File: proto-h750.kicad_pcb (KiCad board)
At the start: 2 copper layers, 63.5 x 73.7 mm, 64 parts, among them J1 Micro_SD_Card, J2 USB_B_Micro, J3 USB_B_Micro, J4 Conn_02x14_Odd_Even, J5 Conn_02x14_Odd_Even, J6 Conn_02x08_Odd_Even, J7 Conn_02x02_Odd_Even, J8 USB_B_Micro, J9 Conn_02x04_Odd_Even, SW1 SW_Push, SW2 SW_Push, SW3 SW_DIP_x01, U1 S25FL132K0XMFI010, U2 STM32H750VBT6, U3 AP1117-33, U4 KSZ8081RNA, Y1 16MHz, Y2 32.768KHz

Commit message: More TX
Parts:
- added REF** (x4): SOP65P1420X343-36N, SOP65P1420X343-36N, F.Cu at (0.00, 0.00)

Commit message: Before deleting Flash
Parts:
- removed REF** (x4): SOP65P1420X343-36N, SOP65P1420X343-36N
- added C25: 10n, Capacitor_SMD:C_0805_2012Metric_Pad1.15x1.40mm_HandSolder, F.Cu at (202.1, 56.4)
- added C26: 100n, Capacitor_SMD:C_0805_2012Metric_Pad1.15x1.40mm_HandSolder, F.Cu at (170.2, 150.4)
- added C27: 220n, Capacitor_SMD:C_0805_2012Metric_Pad1.15x1.40mm_HandSolder, F.Cu at (170.2, 153.4)
- added C28: 100n, Capacitor_SMD:C_0805_2012Metric_Pad1.15x1.40mm_HandSolder, F.Cu at (168.9, 158.1)
- added C29: 100n, Capacitor_SMD:C_0805_2012Metric_Pad1.15x1.40mm_HandSolder, F.Cu at (174.9, 150.4)
- added C30: 1u, Capacitor_SMD:C_0805_2012Metric_Pad1.15x1.40mm_HandSolder, F.Cu at (174.9, 153.4)
- added C31: 100n, Capacitor_SMD:C_0805_2012Metric_Pad1.15x1.40mm_HandSolder, F.Cu at (168.9, 161.0)
- added C32: 100n, Capacitor_SMD:C_0805_2012Metric_Pad1.15x1.40mm_HandSolder, F.Cu at (173.6, 156.3)
- added C33: 220n, Capacitor_SMD:C_0805_2012Metric_Pad1.15x1.40mm_HandSolder, F.Cu at (173.6, 159.3)
- added C34: 1u, Capacitor_SMD:C_0805_2012Metric_Pad1.15x1.40mm_HandSolder, F.Cu at (168.9, 164.0)
- added C35: 330p, Capacitor_SMD:C_0805_2012Metric_Pad1.15x1.40mm_HandSolder, F.Cu at (178.4, 156.3)
- added C36: 220u, Capacitor_SMD:CP_Elec_8x10, F.Cu at (160.7, 161.5)
- added C37: 100n, Capacitor_SMD:C_0805_2012Metric_Pad1.15x1.40mm_HandSolder, F.Cu at (176.1, 146.2)
- added C38: 100n, Capacitor_SMD:C_0805_2012Metric_Pad1.15x1.40mm_HandSolder, F.Cu at (173.6, 162.2)
- added C39: 220n polyester, Capacitor_SMD:C_1812_4532Metric_Pad1.30x3.40mm_HandSolder, F.Cu at (143.9, 160.8)
- added C40: 10n, Capacitor_SMD:C_0805_2012Metric_Pad1.15x1.40mm_HandSolder, F.Cu at (131.0, 155.1)
- added C41: C, Capacitor_SMD:C_0805_2012Metric_Pad1.15x1.40mm_HandSolder, F.Cu at (122.8, 161.5)
- added C42: 10n, Capacitor_SMD:C_0805_2012Metric_Pad1.15x1.40mm_HandSolder, F.Cu at (126.2, 158.0)
- added C43: 10p, Capacitor_SMD:C_0805_2012Metric_Pad1.15x1.40mm_HandSolder, F.Cu at (132.2, 152.1)
- added C44: 100n, Capacitor_SMD:C_0805_2012Metric_Pad1.15x1.40mm_HandSolder, F.Cu at (118.0, 164.5)
- added C45: 100n, Capacitor_SMD:C_0805_2012Metric_Pad1.15x1.40mm_HandSolder, F.Cu at (131.2, 146.2)
- added C46: 100n, Capacitor_SMD:C_0805_2012Metric_Pad1.15x1.40mm_HandSolder, F.Cu at (113.3, 163.2)
- added C47: 100n, Capacitor_SMD:C_0805_2012Metric_Pad1.15x1.40mm_HandSolder, F.Cu at (121.5, 155.6)
- added C48: 10n, Capacitor_SMD:C_0805_2012Metric_Pad1.15x1.40mm_HandSolder, F.Cu at (127.5, 152.1)
- added C49: 0, Capacitor_SMD:C_0805_2012Metric_Pad1.15x1.40mm_HandSolder, F.Cu at (113.3, 166.2)
- added C50: 100n, Capacitor_SMD:C_0805_2012Metric_Pad1.15x1.40mm_HandSolder, F.Cu at (121.5, 158.6)
- added C51: 10n, Capacitor_SMD:C_0805_2012Metric_Pad1.15x1.40mm_HandSolder, F.Cu at (131.2, 149.2)
- added C52: 0, Capacitor_SMD:C_0805_2012Metric_Pad1.15x1.40mm_HandSolder, F.Cu at (118.0, 161.5)
- added C53: 10n, Capacitor_SMD:C_0805_2012Metric_Pad1.15x1.40mm_HandSolder, F.Cu at (94.3, 164.0)
- added C54: 100n, Capacitor_SMD:C_0805_2012Metric_Pad1.15x1.40mm_HandSolder, F.Cu at (94.3, 166.9)
- added C55: 10n, Capacitor_SMD:C_0805_2012Metric_Pad1.15x1.40mm_HandSolder, F.Cu at (99.0, 164.0)
- added C56: 100n, Capacitor_SMD:C_0805_2012Metric_Pad1.15x1.40mm_HandSolder, F.Cu at (107.2, 157.3)
- added C57: 10u, Capacitor_SMD:C_Elec_4x5.4, F.Cu at (101.5, 90.8)
- added C58: 1n, Capacitor_SMD:C_0805_2012Metric_Pad1.15x1.40mm_HandSolder, F.Cu at (171.5, 62.6)
- added C59: C, Capacitor_SMD:C_0805_2012Metric_Pad1.15x1.40mm_HandSolder, F.Cu at (98.1, 33.6)
- added D3: D, Diode_SMD:D_SOD-123, F.Cu at (185.6, 62.3)
- added D4: MMBD914LT3G, Diode_SMD:D_SOD-123, F.Cu at (192.1, 56.5)
- added L1: NRH3012T100MN, Inductor_SMD:L_Taiyo-Yuden_NR-30xx_HandSoldering, F.Cu at (100.8, 68.1)
- added L2: 47u SRR1210-470M, Inductor_SMD:L_Bourns_SRR1210A, F.Cu at (147.5, 151.5)
- added L3: 10u, Inductor_SMD:L_0805_2012Metric_Pad1.15x1.40mm_HandSolder, F.Cu at (126.2, 155.1)
- added L4: 10u, Inductor_SMD:L_0805_2012Metric_Pad1.15x1.40mm_HandSolder, F.Cu at (118.0, 152.7)
- added Q1: BS170, Package_TO_SOT_THT:TO-92_Inline, F.Cu at (184.7, 58.1)
- added Q2: BS170, Package_TO_SOT_THT:TO-92_Inline, F.Cu at (191.2, 52.3)
- added Q3: BS170, Package_TO_SOT_THT:TO-92_Inline, F.Cu at (184.7, 52.3)
- added Q4: IRF540N, Package_TO_SOT_THT:TO-220-3_Vertical, F.Cu at (185.9, 47.0)
- added Q5: BSS138, Package_TO_SOT_SMD:SOT-23, F.Cu at (200.2, 60.2)
- added Q6: MMBT2222, Package_TO_SOT_SMD:SOT-23, F.Cu at (130.8, 158.8)
- added R17: 0, Resistor_SMD:R_0805_2012Metric_Pad1.15x1.40mm_HandSolder, F.Cu at (113.2, 152.7)
- added R18: 10k, Resistor_SMD:R_0805_2012Metric_Pad1.15x1.40mm_HandSolder, F.Cu at (121.7, 146.2)
- added R19: 3k3, Resistor_SMD:R_0805_2012Metric_Pad1.15x1.40mm_HandSolder, F.Cu at (99.0, 166.9)
- added R20: 100, Resistor_SMD:R_0805_2012Metric_Pad1.15x1.40mm_HandSolder, F.Cu at (103.8, 164.0)
- added R21: 10k, Resistor_SMD:R_0805_2012Metric_Pad1.15x1.40mm_HandSolder, F.Cu at (107.2, 160.3)
- added R22: 10k, Resistor_SMD:R_0805_2012Metric_Pad1.15x1.40mm_HandSolder, F.Cu at (112.0, 157.3)
- added R23: 100, Resistor_SMD:R_0805_2012Metric_Pad1.15x1.40mm_HandSolder, F.Cu at (122.8, 164.5)
- added R24: 100k, Resistor_SMD:R_0805_2012Metric_Pad1.15x1.40mm_HandSolder, F.Cu at (121.7, 149.2)
- added R25: 0, Resistor_SMD:R_0805_2012Metric_Pad1.15x1.40mm_HandSolder, F.Cu at (103.8, 166.9)
- added R26: 100, Resistor_SMD:R_0805_2012Metric_Pad1.15x1.40mm_HandSolder, F.Cu at (126.4, 146.2)
- added R27: 100k, Resistor_SMD:R_0805_2012Metric_Pad1.15x1.40mm_HandSolder, F.Cu at (112.0, 160.3)
- added R28: 100, Resistor_SMD:R_0805_2012Metric_Pad1.15x1.40mm_HandSolder, F.Cu at (108.5, 163.2)
- added R29: 62k, Resistor_SMD:R_0805_2012Metric_Pad1.15x1.40mm_HandSolder, F.Cu at (118.0, 167.4)
- added R30: 150k, Resistor_SMD:R_0805_2012Metric_Pad1.15x1.40mm_HandSolder, F.Cu at (116.7, 155.6)
- added R31: 100, Resistor_SMD:R_0805_2012Metric_Pad1.15x1.40mm_HandSolder, F.Cu at (122.7, 152.1)
- added R32: 2k2, Resistor_SMD:R_0805_2012Metric_Pad1.15x1.40mm_HandSolder, F.Cu at (116.7, 158.6)
- added R33: 0, Resistor_SMD:R_0805_2012Metric_Pad1.15x1.40mm_HandSolder, F.Cu at (108.5, 166.2)
- added R34: 0, Resistor_SMD:R_0805_2012Metric_Pad1.15x1.40mm_HandSolder, F.Cu at (126.4, 149.2)
- added R35: 0, Resistor_SMD:R_1210_3225Metric_Pad1.42x2.65mm_HandSolder, F.Cu at (143.2, 165.4)
- added R36: 0, Resistor_SMD:R_1210_3225Metric_Pad1.42x2.65mm_HandSolder, F.Cu at (150.5, 160.4)
- added R37: 10k, Resistor_SMD:R_1210_3225Metric_Pad1.42x2.65mm_HandSolder, F.Cu at (126.4, 91.2)
- added R38: 10k, Resistor_SMD:R_1210_3225Metric_Pad1.42x2.65mm_HandSolder, F.Cu at (106.7, 88.9)
- added R39: 10k, Resistor_SMD:R_1210_3225Metric_Pad1.42x2.65mm_HandSolder, F.Cu at (92.8, 34.2)
- added T1: Transformer_1P_1S, Transformer_THT:Transformer_Toroid_Horizontal_D10.5mm_Amidon-T37, F.Cu at (70.5, 150.5)
- added TP2: TestPoint, TestPoint:TestPoint_Pad_2.0x2.0mm, F.Cu at (195.2, 63.2)
- added TP3: TestPoint, TestPoint:TestPoint_Pad_2.0x2.0mm, F.Cu at (135.1, 158.6)
- added TP4: TestPoint, TestPoint:TestPoint_Pad_2.0x2.0mm, F.Cu at (127.2, 167.0)
- added U10: BGA2869, Package_TO_SOT_SMD:SOT-363_SC-70-6, F.Cu at (122.5, 167.9)
- added U11: BGA2869, Package_TO_SOT_SMD:SOT-363_SC-70-6, F.Cu at (127.3, 163.0)
- added U5: LM7812_TO220, Package_TO_SOT_THT:TO-220-3_Vertical, F.Cu at (197.5, 47.0)
- added U6: LM5134AMF_NOPB, Package_TO_SOT_SMD:SOT-23-6_Handsoldering, F.Cu at (208.7, 45.4)
- added U8: STA510, Package_SO:ST_PowerSSO-36_SlugDown, F.Cu at (161.2, 150.7)
- added U9: SA612, Package_SO:SOIC-8_3.9x4.9mm_P1.27mm, F.Cu at (115.1, 148.0)
- added X1: ASV-xxxMHz, Oscillator:Oscillator_SMD_Abracon_ASV-4Pin_7.0x5.1mm, F.Cu at (98.3, 84.3)
- C1, C10, C12, C13, C14, C15, C16, C17, C18, C2, C23, C3, C4, C5, C6, C7, C8: footprint Capacitor_SMD:C_0805_2012Metric -> Capacitor_SMD:C_0805_2012Metric_Pad1.15x1.40mm_HandSolder
- C11: value 18p -> 1u; footprint Capacitor_SMD:C_0805_2012Metric -> Capacitor_SMD:C_0805_2012Metric_Pad1.15x1.40mm_HandSolder
- C19: value 100n -> 10u; footprint Capacitor_SMD:C_0805_2012Metric -> Capacitor_SMD:C_0805_2012Metric_Pad1.15x1.40mm_HandSolder
- C20: value 2.2u -> 10u; footprint Capacitor_SMD:C_0805_2012Metric -> Capacitor_SMD:C_0805_2012Metric_Pad1.15x1.40mm_HandSolder
- C21: value 4.7u -> 10u; footprint Capacitor_SMD:C_0805_2012Metric -> Capacitor_SMD:C_0805_2012Metric_Pad1.15x1.40mm_HandSolder
- C22: value 100n -> 1u; footprint Capacitor_SMD:C_0805_2012Metric -> Capacitor_SMD:C_0805_2012Metric_Pad1.15x1.40mm_HandSolder
- C24: value 4.7u -> 100n; footprint Capacitor_SMD:C_0805_2012Metric -> Capacitor_SMD:C_0805_2012Metric_Pad1.15x1.40mm_HandSolder
- C9: value 18p -> 10u; footprint Capacitor_SMD:C_0805_2012Metric -> Capacitor_SMD:C_Elec_4x5.4
- J1: value Micro_SD_Card -> Conn_02x14_Odd_Even; footprint Connector_Card:microSD_HC_Hirose_DM3AT-SF-PEJM5 -> Connector_PinHeader_2.54mm:PinHeader_2x14_P2.54mm_Vertical
- J5: value Conn_02x14_Odd_Even -> Conn_02x08_Odd_Even; footprint Connector_PinHeader_2.54mm:PinHeader_2x14_P2.54mm_Vertical -> Connector_PinHeader_2.54mm:PinHeader_2x08_P2.54mm_Vertical
- J6: value Conn_02x08_Odd_Even -> AudioJack3; footprint Connector_PinHeader_2.54mm:PinHeader_2x08_P2.54mm_Vertical -> Connector_Audio:Jack_3.5mm_CUI_SJ1-3535NG_Horizontal
- J8: value USB_B_Micro -> Conn_02x08_Odd_Even; footprint Connector_USB:USB_Micro-B_Molex-105017-0001 -> Connector_PinHeader_2.54mm:PinHeader_2x08_P2.54mm_Vertical
- J9: value Conn_02x04_Odd_Even -> AudioJack3; footprint Connector_PinHeader_2.54mm:PinHeader_2x04_P2.54mm_Vertical -> Connector_Audio:Jack_3.5mm_CUI_SJ1-3535NG_Horizontal
- R1, R16, R2, R3: footprint Resistor_SMD:R_0805_2012Metric -> Resistor_SMD:R_0805_2012Metric_Pad1.15x1.40mm_HandSolder
- R10, R12: value 0R -> 10k; footprint Resistor_SMD:R_2010_5025Metric -> Resistor_SMD:R_0805_2012Metric_Pad1.15x1.40mm_HandSolder
- R11: value 0R -> 330; footprint Resistor_SMD:R_2010_5025Metric -> Resistor_SMD:R_0805_2012Metric_Pad1.15x1.40mm_HandSolder
- R13: value 0R -> 10K; footprint Resistor_SMD:R_2010_5025Metric -> Resistor_SMD:R_0805_2012Metric_Pad1.15x1.40mm_HandSolder
- R14: value 0R -> 20 0.25W; footprint Resistor_SMD:R_2010_5025Metric -> Resistor_SMD:R_1210_3225Metric_Pad1.42x2.65mm_HandSolder
- R15: value 0R -> 6.2 0.25 W; footprint Resistor_SMD:R_2010_5025Metric -> Resistor_SMD:R_1210_3225Metric_Pad1.42x2.65mm_HandSolder
- R4, R5: value 10K -> 0; footprint Resistor_SMD:R_0805_2012Metric -> Resistor_SMD:R_0805_2012Metric_Pad1.15x1.40mm_HandSolder
- R6: value 10K -> 10k; footprint Resistor_SMD:R_0805_2012Metric -> Resistor_SMD:R_0805_2012Metric_Pad1.15x1.40mm_HandSolder
- R7: value 6.49K 1% -> 10k; footprint Resistor_SMD:R_0805_2012Metric -> Resistor_SMD:R_0805_2012Metric_Pad1.15x1.40mm_HandSolder
- R8: value 0R -> 2.2; footprint Resistor_SMD:R_2010_5025Metric -> Resistor_SMD:R_0805_2012Metric_Pad1.15x1.40mm_HandSolder
- R9: value 0R -> 1K; footprint Resistor_SMD:R_2010_5025Metric -> Resistor_SMD:R_0805_2012Metric_Pad1.15x1.40mm_HandSolder
- U4: value KSZ8081RNA -> LM7805_TO220; footprint Package_DFN_QFN:QFN-24-1EP_4x4mm_P0.5mm_EP2.6x2.6mm -> Package_TO_SOT_THT:TO-220-3_Vertical
- Y2: value 32.768KHz -> ECS-10.7-7.5B; footprint Crystal:Crystal_SMD_MicroCrystal_CC8V-T1A-2Pin_2.0x1.2mm_HandSoldering -> Crystal:Crystal_HC49-U-3Pin_Vertical
- moved H1 144.6 mm to (58.4, 149.9)
- moved R13 109.7 mm to (214.0, 44.6), turned to 0 degrees
- moved Y2 95.3 mm to (95.9, 159.2), turned to 0 degrees
- moved H3 95.1 mm to (193.9, 84.2)
- moved R8 90.8 mm to (208.2, 49.2), turned to 0 degrees
- moved R9 88.4 mm to (202.8, 50.5), turned to 0 degrees
- moved R10 85.4 mm to (198.1, 53.5), turned to 0 degrees
- moved C24 84.0 mm to (207.6, 52.2)
- moved J8 79.2 mm to (180.3, 72.4), turned to 0 degrees
- moved C22 78.1 mm to (202.8, 53.5)
- moved R11 77.8 mm to (190.8, 62.1), turned to 0 degrees
- moved R12 77.0 mm to (185.1, 65.5), turned to 0 degrees
- moved R6 76.6 mm to (198.1, 50.5), turned to 0 degrees
- moved R14 74.0 mm to (149.2, 165.4), turned to 0 degrees
- moved J6 72.3 mm to (87.6, 110.5), turned to 90 degrees
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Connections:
- C1 pad 1: VCC -> /VCC_CPU
- C10 pad 1: VCC -> /VCC_CPU
- C11 pad 1: GND -> Net-(C11-Pad1)
- C11 pad 2: Net-(C11-Pad2) -> GND
- C12 pad 1: VCC -> /VCC_CPU
- C13 pad 1: VCC -> /VCC_CPU
- C14 pad 1: GND -> Net-(C11-Pad1)
- C14 pad 2: VCC -> GND
- C15 pad 1: VCC -> /VCC_CPU
- C19 pad 1: GND -> +24V
- C19 pad 2: Net-(C19-Pad2) -> GND
- C20 pad 1: GND -> Net-(C20-Pad1)
- C20 pad 2: Net-(C20-Pad2) -> GND
- C21 pad 1: GND -> +24V
- C21 pad 2: Net-(C20-Pad2) -> GND
- C22 pad 1: GND -> /TX/+12V
- C22 pad 2: VCC -> GND
- C23 pad 1: GND -> /TX/+12V
- C23 pad 2: VCC -> GND
- C24 pad 1: GND -> /TX/+12V
- C24 pad 2: VCC -> GND
- C4 pad 1: VCC -> /VCC_CPU
- C7 pad 1: VCC -> /VCC_CPU
- C8 pad 1: VCC -> /VCC_CPU
- C9 pad 1: GND -> /AudioOut
- J1 pad 1: Net-(J1-Pad1) -> /PC0
- J1 pad 10: (no net) -> /PA5
- J1 pad 11: (no net) -> /PA6
- J1 pad 2: Net-(J1-Pad2) -> /PC1
- J1 pad 3: /SD_CMD -> /PC2
- J1 pad 4: VCC -> TXV
- J1 pad 5: /SD_CK -> /PA0
- J1 pad 6: GND -> /PA1
- J1 pad 7: /SD_D0 -> /PA2
- J1 pad 8: Net-(J1-Pad8) -> /PA3
- J1 pad 9: GND -> /AudioOut
- J2 pad 1: +5V -> Net-(J2-Pad1)
- J2 pad 4: Net-(J2-Pad4) -> (no net)
- J3 pad 1: +5V -> Net-(J2-Pad1)
- J3 pad 4: Net-(J3-Pad4) -> (no net)
- J4 pad 1: /PC0 -> GND
- J4 pad 10: /PA5 -> TX_ENA
- J4 pad 11: /PA6 -> /PE1
- J4 pad 12: /PA7 -> RXTX
- J4 pad 13: /PC4 -> /PB9
- J4 pad 14: /PC5 -> /PB8
- J4 pad 15: /PB0 -> /PB7
- J4 pad 16: /PB1 -> /PB6
- J4 pad 17: /PE11 -> /PB5
- J4 pad 18: /PE12 -> /PB4
- J4 pad 19: /PE13 -> /PB3
- J4 pad 2: /ENET_MDC -> +5V
- J4 pad 20: /PE14 -> /PD7
- J4 pad 21: /PE15 -> /PD6
- J4 pad 22: /PB10 -> /PD5
- J4 pad 23: /PB11 -> /PD4
- J4 pad 24: /PB12 -> /PD3
- J4 pad 25: /PB13 -> /PD1
- J4 pad 26: GND -> /PD0
- J4 pad 27: GND -> /PC10
- J4 pad 28: GND -> /PA15
- J4 pad 3: /PC2 -> VCC
- J4 pad 4: /PC3 -> /nRESET
- J4 pad 5: /PA0 -> VCC
- J4 pad 6: /PA1 -> /PE6
- J4 pad 7: /ENET_MDIO -> /PE5
- J4 pad 8: /PA3 -> /PE4
- J4 pad 9: /PA4 -> /PE3
- J5 pad 1: GND -> /PA9
- J5 pad 10: /PE2 -> /PD13
- J5 pad 11: /PE1 -> /PD10
- J5 pad 12: /PE0 -> /PD11
- J5 pad 13: /PB9 -> /PD8
- J5 pad 14: /PB8 -> /PD9
- J5 pad 15: /PB7 -> GND
- J5 pad 16: /PB6 -> GND
- J5 pad 2: +5V -> /PA10
- J5 pad 3: VCC -> MCO
- J5 pad 4: /nRESET -> /PA8
- J5 pad 5: VCC -> A_PWM
- J5 pad 6: /PE6 -> /PC7
- J5 pad 7: /PE5 -> /PD14
- J5 pad 8: /PE4 -> /PD15
- J5 pad 9: /PE3 -> /PD12
- J8 pad 1: +5V -> +24V
- J8 pad 2: Net-(J8-Pad2) -> (no net)
- J8 pad 3: Net-(J8-Pad3) -> +24V
- J8 pad 4: Net-(J8-Pad4) -> (no net)
- J8 pad 5: GND -> MODUL_OUT
- J8 pad 6: GND -> (no net)
- R10 pad 1: /ENET_TXD1 -> Net-(J8-Pad11)
- R10 pad 2: /PB13 -> Net-(D3-Pad2)
- R11 pad 1: /ENET_RXD0 -> Net-(D3-Pad2)
- R11 pad 2: /PC4 -> GND
- R12 pad 1: /ENET_RXD1 -> TXV
- R12 pad 2: /PA5 -> GND
- R13 pad 1: Net-(R13-Pad1) -> RXTX
- R13 pad 2: /PA7 -> GND
- R14 pad 1: /ENET_CLK -> Net-(L2-Pad1)
- R14 pad 2: /PA1 -> Net-(C35-Pad1)
- R15 pad 1: Net-(R13-Pad1) -> MODUL_OUT
- R15 pad 2: /ENET_CRSDV -> Net-(C37-Pad1)
- R4 pad 1: VCC -> Net-(J2-Pad1)
- R4 pad 2: /ENET_MDIO -> +5V
- R5 pad 1: VCC -> +5V
- R5 pad 2: /ENET_MDC -> Net-(C20-Pad1)
- R6 pad 2: Net-(C19-Pad2) -> TX_ENA
- R7 pad 1: GND -> MCO
- R7 pad 2: Net-(R7-Pad2) -> GND
- R8 pad 1: /ENET_TXEN -> Net-(C59-Pad2)
- R8 pad 2: /PB11 -> Net-(R8-Pad2)
- R9 pad 1: /ENET_TXD0 -> Net-(C59-Pad1)
- R9 pad 2: /PB12 -> GND
- U1 pad 8: VCC -> /VCC_CPU
- U2 pad 1: /PE2 -> TX_ENA
- U2 pad 100: VCC -> /VCC_CPU
- U2 pad 11: VCC -> /VCC_CPU
- U2 pad 16: /ENET_MDC -> /PC1
- U2 pad 18: /PC3 -> TXV
- U2 pad 20: VCC -> Net-(C11-Pad1)
- U2 pad 21: VCC -> /VCC_CPU
- U2 pad 24: /ENET_MDIO -> /PA2
- U2 pad 27: VCC -> /VCC_CPU
- U2 pad 28: /PA4 -> /AudioOut
- U2 pad 31: /PA7 -> /Microphone
- U2 pad 35: /PB1 -> RF_ADC_IN
- U2 pad 41: /PE11 -> A_PWM
- U2 pad 42: /PE12 -> A_PWRDN
- U2 pad 43: /PE13 -> A_FAULT
- U2 pad 50: VCC -> /VCC_CPU
- U2 pad 6: VCC -> /VCC_CPU
- U2 pad 63: /PC6 -> A_PWM
- U2 pad 65: /SD_D0 -> (no net)
- U2 pad 66: /PC9 -> MCO
- U2 pad 75: VCC -> /VCC_CPU
- U2 pad 8: Net-(C11-Pad2) -> (no net)
- U2 pad 80: /SD_CK -> (no net)
- U2 pad 83: /SD_CMD -> (no net)
- U2 pad 9: Net-(C9-Pad2) -> (no net)
- U2 pad 97: /PE0 -> RXTX
- U4 pad 1: Net-(C20-Pad2) -> +24V
- U4 pad 2: VCC -> GND
- U4 pad 3: /ETH_RX- -> Net-(C20-Pad1)
- Y1 pad 2: Net-(Y1-Pad2) -> (no net)
- Y1 pad 4: Net-(Y1-Pad4) -> (no net)
- Y2 pad 1: Net-(C11-Pad2) -> Net-(C48-Pad1)
- Y2 pad 2: Net-(C9-Pad2) -> GND
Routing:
- net VCC: track 221.0 -> 27.9 mm, vias 7 -> 0
- net +5V: track 127.9 -> 27.2 mm, vias 6 -> 0
- net /ENET_MDC: track 80.3 -> 0.00 mm
- net /ENET_MDIO: track 70.6 -> 0.00 mm
- net GND: track 127.8 -> 183.8 mm, vias 44 -> 19
- net /BOOT: track 46.8 -> 0.00 mm, vias 2 -> 0
- net /ENET_CLK: track 46.1 -> 0.00 mm
- net /VCC_CPU: track 0.00 -> 44.9 mm
- net /PB13: track 40.0 -> 0.00 mm
- net /PB12: track 35.0 -> 0.00 mm
- net /PC0: track 34.9 -> 0.00 mm
- net /USB0_D+: track 34.8 -> 0.00 mm
- net /USB0_D-: track 34.7 -> 0.00 mm
- net /PA1: track 32.5 -> 0.00 mm
- net /PC2: track 32.0 -> 0.00 mm
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- removed copper zone on B.Cu, net +5V
- removed copper zone on B.Cu, net GND
- removed copper zone on F.Cu, net GND
- removed copper zone on F.Cu, net VCC
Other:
- board outline removed
- board text removed: "BOOT0"
- board text removed: "PA8"
- board text removed: "RESET"
- board text removed: "WKP"

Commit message: More routing
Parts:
- removed C1: 100n, Capacitor_SMD:C_0805_2012Metric_Pad1.15x1.40mm_HandSolder
- removed U1: S25FL132K0XMFI010, Package_SO:SO-8_5.3x6.2mm_P1.27mm
- added TP13: TestPoint_Small, TestPoint:TestPoint_Pad_D1.0mm, F.Cu at (105.2, 86.6)
- added TP14: TestPoint_Small, TestPoint:TestPoint_Pad_D1.0mm, F.Cu at (107.4, 82.8)
- added TP15: TestPoint_Small, TestPoint:TestPoint_Pad_D1.0mm, F.Cu at (109.2, 86.6)
- added TP16: TestPoint_Small, TestPoint:TestPoint_Pad_D1.0mm, F.Cu at (107.2, 86.6)
- added TP17: TestPoint_Small, TestPoint:TestPoint_Pad_D1.0mm, F.Cu at (111.3, 86.6)
- J1: value Conn_02x14_Odd_Even -> Conn_02x08_Odd_Even; footprint Connector_PinHeader_2.54mm:PinHeader_2x14_P2.54mm_Vertical -> Connector_PinHeader_2.54mm:PinHeader_2x08_P2.54mm_Vertical
- TP2, TP3, TP4: footprint TestPoint:TestPoint_Pad_2.0x2.0mm -> TestPoint:TestPoint_Pad_D1.0mm
- moved C3 61.7 mm to (121.4, 85.9), turned to 270 degrees
- moved C11 46.4 mm to (103.9, 80.3), turned to 180 degrees
- moved C10 30.9 mm to (126.5, 68.1)
- moved D2 26.6 mm to (168.3, 82.8)
- moved R37 22.9 mm to (103.9, 95.5)
- moved U8 20.3 mm to (158.5, 130.6)
- moved J1 7.62 mm to (110.0, 96.8)
- moved J2 5.43 mm to (147.6, 86.1)
- moved J3 5.43 mm to (147.6, 75.9)
- moved R38 1.61 mm to (107.2, 90.4)
- moved C4 1.52 mm to (103.9, 82.3)
- moved C57 0.38 mm to (101.5, 91.2)
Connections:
- J1 pad 1: /PC0 -> /PA6
- J1 pad 10: /PA5 -> /PE14
- J1 pad 11: /PA6 -> /PE15
- J1 pad 12: /Microphone -> /PB10
- J1 pad 13: /PC4 -> /PB11
- J1 pad 14: /PC5 -> /PB12
- J1 pad 15: /PB0 -> /PB13
- J1 pad 16: RF_ADC_IN -> GND
- J1 pad 2: /PC1 -> /Microphone
- J1 pad 3: /PC2 -> TXV
- J1 pad 4: TXV -> /PC5
- J1 pad 5: /PA0 -> /PB0
- J1 pad 6: /PA1 -> RF_ADC_IN
- J1 pad 7: /PA2 -> A_PWM
- J1 pad 8: /PA3 -> A_PWRDN
- J1 pad 9: /AudioOut -> A_FAULT
- R16 pad 1: VCC -> /VCC_CPU
- R37 pad 1: VCC -> /VCC_CPU
- U2 pad 15: /PC0 -> (no net)
- U2 pad 16: /PC1 -> (no net)
- U2 pad 17: /PC2 -> (no net)
- U2 pad 18: TXV -> (no net)
- U2 pad 32: /PC4 -> TXV
- U2 pad 36: /SCLK -> (no net)
- U2 pad 37: /IO0 -> (no net)
- U2 pad 38: /IO1 -> (no net)
- U2 pad 39: /IO2 -> (no net)
- U2 pad 40: /IO3 -> (no net)
- U2 pad 79: /nCS -> (no net)
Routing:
- net /VCC_CPU: track 44.9 -> 157.0 mm, vias 0 -> 2
- net GND: track 183.8 -> 244.2 mm, vias 19 -> 24
- net /nRESET: track 109.1 -> 146.5 mm
- net /PA6: track 0.00 -> 34.0 mm
- net /SCLK: track 29.5 -> 0.00 mm
- net /IO0: track 23.1 -> 0.00 mm
- net /PB13: track 0.00 -> 19.1 mm
- net /PB11: track 0.00 -> 16.6 mm
- net TXV: track 0.00 -> 16.1 mm
- net /PE15: track 0.00 -> 15.9 mm
- net A_PWM: track 0.00 -> 15.3 mm
- net A_FAULT: track 0.00 -> 15.2 mm
- net /PB0: track 0.00 -> 15.1 mm
- net /PB12: track 0.00 -> 14.3 mm
- net /PB10: track 0.00 -> 13.1 mm
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
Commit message: RX placed
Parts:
- moved C43 68.6 mm to (115.6, 85.6), turned to 270 degrees
- moved R23 64.5 mm to (109.7, 101.3)
- moved TP4 63.4 mm to (83.5, 121.1)
- moved C44 61.2 mm to (109.7, 103.9), turned to 180 degrees
- moved U10 59.7 mm to (113.0, 109.0), turned to 180 degrees
- moved R21 59.3 mm to (113.8, 101.3)
- moved TP3 57.9 mm to (114.8, 104.4)
- moved C54 57.4 mm to (114.2, 113.0), turned to 180 degrees
- moved R22 56.3 mm to (117.9, 101.3)
- moved R29 55.3 mm to (89.5, 120.1)
- moved T1 54.5 mm to (122.8, 135.4), turned to 90 degrees
- moved U11 52.9 mm to (107.3, 114.1), turned to 180 degrees
- moved Q6 52.3 mm to (94.0, 121.7)
- moved C52 50.7 mm to (83.6, 124.3), turned to 90 degrees
- moved C50 49.4 mm to (119.9, 109.2), turned to 180 degrees
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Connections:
- T1 pad 1: Net-(C40-Pad1) -> GND
- T1 pad 2: GND -> Net-(C40-Pad1)
- T1 pad 3: Net-(C41-Pad1) -> Net-(T1-Pad3)
- T1 pad 4: Net-(T1-Pad4) -> Net-(C41-Pad1)
- U9 pad 1: Net-(T1-Pad4) -> Net-(T1-Pad3)
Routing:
- net GND: track 244.2 -> 345.7 mm, vias 24 -> 36
- net RF_ADC_IN: track 12.2 -> 28.7 mm
- net Net-(C50-Pad1): track 0.00 -> 9.57 mm
- net Net-(C54-Pad1): track 0.00 -> 8.54 mm
- net +5V: track 27.2 -> 34.2 mm
- net Net-(C51-Pad1): track 0.00 -> 6.44 mm
- net Net-(C45-Pad1): track 0.00 -> 5.19 mm
- net Net-(C55-Pad1): track 0.00 -> 4.76 mm
- net Net-(C44-Pad1): track 0.00 -> 4.55 mm
- net Net-(C47-Pad1): track 0.00 -> 3.32 mm
- net Net-(C55-Pad2): track 0.00 -> 2.30 mm
- net Net-(C51-Pad2): track 0.00 -> 1.79 mm

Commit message: -
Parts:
- removed J2: USB_B_Micro, Connector_USB:USB_Micro-B_Molex-105017-0001
- removed U8: STA510, Package_SO:ST_PowerSSO-36_SlugDown
- added U1: STA516BETR, footprints:SOP65P1420X343-36N, F.Cu at (165.0, 130.4)
- SW1, SW2: value SW_Push -> SW_DIP_x01; footprint Button_Switch_THT:SW_Tactile_SPST_Angled_PTS645Vx31-2LFS -> Connector_PinHeader_2.54mm:PinHeader_1x02_P2.54mm_Vertical
- moved D1 28.7 mm to (159.0, 81.5)
- moved SW2 16.3 mm to (87.1, 75.3), turned to 0 degrees
- moved SW1 2.64 mm to (87.2, 82.8), turned to 0 degrees
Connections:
- SW1 pad 2: /PC13 -> /nRESET
- SW2 pad 2: /nRESET -> /PC13
- U2 pad 53: /USB0_D- -> (no net)
- U2 pad 54: /USB0_D+ -> (no net)
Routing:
- net /nRESET: track 146.5 -> 149.2 mm

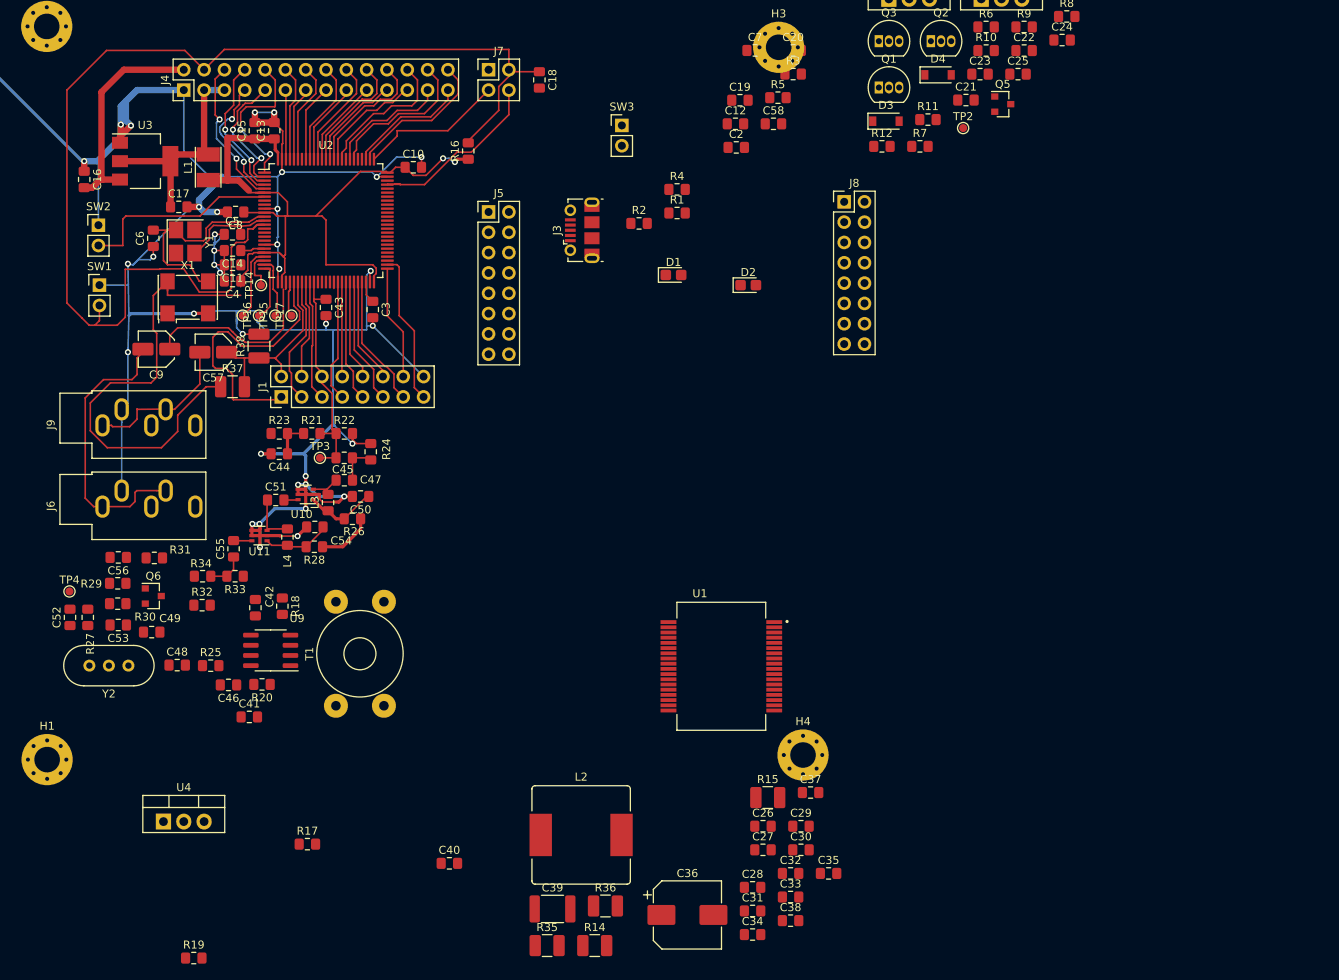
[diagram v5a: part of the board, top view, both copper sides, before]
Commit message: RX routed
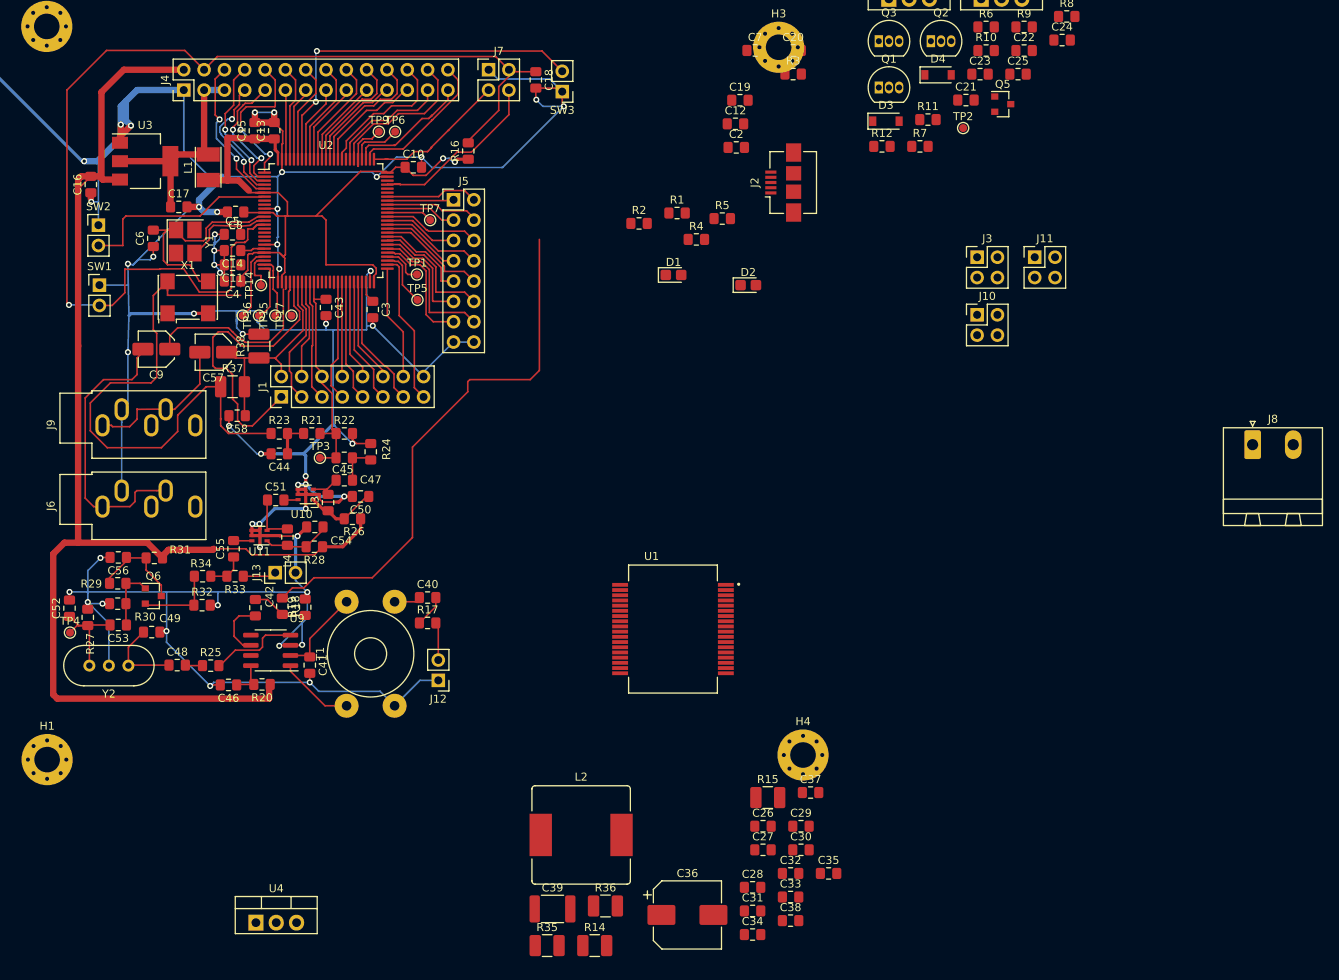
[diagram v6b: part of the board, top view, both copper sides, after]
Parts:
- added J10: Conn_02x02_Odd_Even, Connector_PinHeader_2.54mm:PinHeader_2x02_P2.54mm_Vertical, F.Cu at (197.0, 86.5)
- added J11: Conn_02x02_Odd_Even, Connector_PinHeader_2.54mm:PinHeader_2x02_P2.54mm_Vertical, F.Cu at (204.2, 79.3)
- added J12: Conn_01x02, Connector_PinHeader_2.54mm:PinHeader_1x02_P2.54mm_Vertical, F.Cu at (129.6, 132.2)
- added J13: Conn_01x02, Connector_PinHeader_2.54mm:PinHeader_1x02_P2.54mm_Vertical, F.Cu at (109.2, 118.7)
- added J2: USB_B_Micro, Connector_USB:USB_Micro-B_Amphenol_10104110_Horizontal, F.Cu at (172.7, 70.0)
- added TP1: TestPoint, TestPoint:TestPoint_Pad_D1.0mm, F.Cu at (126.9, 81.5)
- added TP5: TestPoint, TestPoint:TestPoint_Pad_D1.0mm, F.Cu at (127.0, 84.6)
- added TP6: TestPoint_Small, TestPoint:TestPoint_Pad_D1.0mm, F.Cu at (124.2, 63.6)
- added TP7: TestPoint_Small, TestPoint:TestPoint_Pad_D1.0mm, F.Cu at (128.6, 74.7)
- added TP9: TestPoint_Small, TestPoint:TestPoint_Pad_D1.0mm, F.Cu at (122.2, 63.6)
- J3: value USB_B_Micro -> Conn_02x02_Odd_Even; footprint Connector_USB:USB_Micro-B_Molex-105017-0001 -> Connector_PinHeader_2.54mm:PinHeader_2x02_P2.54mm_Vertical
- J8: value Conn_02x08_Odd_Even -> Screw_Terminal_01x02; footprint Connector_PinHeader_2.54mm:PinHeader_2x08_P2.54mm_Vertical -> Connector_Phoenix_MSTB:PhoenixContact_MSTBA_2,5_2-G-5,08_1x02_P5.08mm_Horizontal
- moved C58 76.3 mm to (104.5, 99.1), turned to 180 degrees
- moved J8 59.4 mm to (231.4, 102.7)
- moved J3 49.5 mm to (197.0, 79.3), turned to 0 degrees
- moved R19 46.0 mm to (113.0, 123.1), turned to 90 degrees
- moved C40 33.3 mm to (128.3, 121.9)
- moved R17 31.5 mm to (128.3, 125.0)
- moved U4 17.1 mm to (106.8, 162.5)
- moved R5 16.6 mm to (165.1, 74.5)
- moved C41 9.95 mm to (113.5, 130.3), turned to 270 degrees
- moved SW3 8.57 mm to (145.1, 58.6), turned to 180 degrees
- moved U1 7.63 mm to (158.9, 125.8)
- moved R4 6.70 mm to (161.9, 77.1)
- moved TP4 5.14 mm to (83.6, 126.2)
- moved J5 4.64 mm to (131.5, 72.1)
- moved T1 1.33 mm to (124.1, 135.4)
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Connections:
- C10 pad 1: /VCC_CPU -> VCC_CPU
- C12 pad 1: /VCC_CPU -> VCC_CPU
- C13 pad 1: /VCC_CPU -> VCC_CPU
- C15 pad 1: /VCC_CPU -> VCC_CPU
- C4 pad 1: /VCC_CPU -> VCC_CPU
- C7 pad 1: /VCC_CPU -> VCC_CPU
- C8 pad 1: /VCC_CPU -> VCC_CPU
- J1 pad 7: A_PWM -> /PE11
- J3 pad 1: Net-(J3-Pad1) -> MODUL_OUT
- J3 pad 2: /USB1_D- -> GND
- J3 pad 3: /USB1_D+ -> MODUL_OUT
- J3 pad 4: (no net) -> GND
- J8 pad 2: (no net) -> GND
- L1 pad 1: /VCC_CPU -> VCC_CPU
- Q1 pad 1: Net-(J8-Pad11) -> Net-(J10-Pad1)
- Q2 pad 1: Net-(J8-Pad11) -> Net-(J10-Pad1)
- Q3 pad 1: Net-(J8-Pad11) -> Net-(J10-Pad1)
- Q4 pad 2: Net-(J8-Pad11) -> Net-(J10-Pad1)
- R10 pad 1: Net-(J8-Pad11) -> Net-(J10-Pad1)
- R16 pad 1: /VCC_CPU -> VCC_CPU
- R17 pad 2: RF_IN_1 -> Net-(J12-Pad2)
- R23 pad 1: VCC -> VCC_CPU
- R33 pad 1: RF_IN_2 -> Net-(J13-Pad1)
- R37 pad 1: /VCC_CPU -> VCC_CPU
- R4 pad 1: Net-(J3-Pad1) -> Net-(J2-Pad1)
- TP2 pad 1: Net-(J8-Pad11) -> Net-(J10-Pad1)
- U2 pad 100: /VCC_CPU -> VCC_CPU
- U2 pad 11: /VCC_CPU -> VCC_CPU
- U2 pad 21: /VCC_CPU -> VCC_CPU
- U2 pad 27: /VCC_CPU -> VCC_CPU
- U2 pad 41: A_PWM -> /PE11
- U2 pad 50: /VCC_CPU -> VCC_CPU
- U2 pad 53: (no net) -> /USB0_D-
- U2 pad 54: (no net) -> /USB0_D+
- U2 pad 6: /VCC_CPU -> VCC_CPU
- U2 pad 65: (no net) -> /SD_D0
- U2 pad 75: /VCC_CPU -> VCC_CPU
- U2 pad 79: (no net) -> /nCS
- U2 pad 80: (no net) -> /SD_CK
- X1 pad 4: /VCC_CPU -> VCC_CPU
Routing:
- net GND: track 345.4 -> 528.4 mm, vias 36 -> 51
- net VCC_CPU: track 0.00 -> 168.7 mm, vias 0 -> 2
- net /VCC_CPU: track 157.0 -> 0.00 mm, vias 2 -> 0
- net +5V: track 34.2 -> 165.1 mm
- net MCO: track 0.00 -> 76.5 mm
- net /BOOT: track 0.00 -> 46.3 mm, vias 0 -> 2
- net /PD9: track 0.00 -> 17.7 mm
- net /PD11: track 0.00 -> 15.8 mm
- net /PE11: track 0.00 -> 15.3 mm
- net /PD8: track 0.00 -> 15.0 mm
- net /PD13: track 0.00 -> 13.7 mm
- net /PD10: track 0.00 -> 13.6 mm
- net Net-(C52-Pad1): track 0.00 -> 13.3 mm
- net /PD15: track 0.00 -> 12.7 mm
- net Net-(C56-Pad1): track 0.00 -> 12.1 mm
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
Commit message: More rouiting
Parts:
- added C1: 100n, Capacitor_SMD:C_0805_2012Metric_Pad1.15x1.40mm_HandSolder, F.Cu at (123.1, 84.1)
- moved C20 84.2 mm to (141.4, 131.1)
- moved R13 82.3 mm to (144.1, 87.9), turned to 270 degrees
- moved J8 81.4 mm to (153.7, 127.0)
- moved D2 80.8 mm to (91.2, 58.7)
- moved R39 80.7 mm to (161.4, 76.7)
- moved C59 75.5 mm to (162.3, 73.3), turned to 180 degrees
- moved C19 74.6 mm to (145.7, 131.1), turned to 180 degrees
- moved C28 67.4 mm to (129.2, 103.7), turned to 180 degrees
- moved C7 67.3 mm to (104.3, 71.3), turned to 180 degrees
- moved R5 67.0 mm to (135.6, 134.7), turned to 270 degrees
- moved C31 67.0 mm to (129.0, 107.2)
- moved R2 65.0 mm to (91.2, 61.4)
- moved C38 63.3 mm to (162.3, 100.0), turned to 90 degrees
- moved C24 62.3 mm to (148.4, 71.5), turned to 180 degrees
- moved C12 62.0 mm to (109.2, 85.7), turned to 270 degrees
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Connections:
- D4 pad 1: +24V -> /TX/+12V
- R3 pad 1: VCC -> VCC_CPU
- TP2 pad 1: Net-(J10-Pad1) -> TXV
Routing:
- net GND: track 528.4 -> 880.3 mm, vias 51 -> 89
- net +5V: track 165.1 -> 309.1 mm
- net /TX/+12V: track 0.00 -> 47.7 mm
- net Net-(J10-Pad1): track 0.00 -> 45.9 mm, vias 0 -> 1
- net Net-(C59-Pad1): track 0.00 -> 45.0 mm
- net +24V: track 0.00 -> 44.3 mm
- net /USB1_D-: track 0.00 -> 36.9 mm
- net /USB1_D+: track 0.00 -> 35.8 mm
- net MCO: track 76.5 -> 97.4 mm, vias 0 -> 2
- net Net-(L2-Pad1): track 0.00 -> 15.3 mm
- net Net-(R35-Pad2): track 0.00 -> 14.0 mm, vias 0 -> 5
- net VCC_CPU: track 168.7 -> 182.1 mm
- net TXV: track 16.1 -> 29.3 mm
- net MODUL_OUT: track 0.00 -> 10.8 mm
- net /BOOT: track 46.3 -> 57.0 mm
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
